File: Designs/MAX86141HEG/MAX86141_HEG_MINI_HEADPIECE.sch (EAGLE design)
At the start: 6 parts

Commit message: updates/another fix for boot routine
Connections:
- net GPIO1: now also JP4.6
- net GPIO2: now also JP4.5
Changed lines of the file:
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@@
 <setting verticaltext="up"/>
 </settings>
-<grid distance="10" unitdist="mil" unit="mil" style="lines" multiple="1" display="no" altdistance="0.01" altunitdist="inch" altunit="inch"/>
+<grid distance="0.01" unitdist="inch" unit="inch" style="lines" multiple="1" display="no" altdistance="0.01" altunitdist="inch" altunit="inch"/>
 <layers>
 <layer number="1" name="Top" color="4" fill="1" visible="no" active="no"/>
@@
 <label x="-25.146" y="91.948" size="1.778" layer="95"/>
 </segment>
+<segment>
+<pinref part="JP4" gate="A" pin="6"/>
+<wire x1="-86.614" y1="93.472" x2="-86.36" y2="93.472" width="0.1524" layer="91"/>
+<wire x1="-86.36" y1="93.472" x2="-86.36" y2="86.36" width="0.1524" layer="91"/>
+<label x="-87.63" y="86.106" size="1.778" layer="95" rot="R270"/>
+</segment>
 </net>
 <net name="GPIO2" class="0">
@@
 <label x="-25.146" y="89.662" size="1.778" layer="95"/>
 </segment>
+<segment>
+<pinref part="JP4" gate="A" pin="5"/>
+<wire x1="-89.154" y1="93.472" x2="-88.9" y2="93.472" width="0.1524" layer="91"/>
+<wire x1="-88.9" y1="93.472" x2="-88.9" y2="86.36" width="0.1524" layer="91"/>
+<label x="-90.17" y="85.852" size="1.778" layer="95" rot="R270"/>
+</segment>
 </net>

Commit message: quality improvements to design (hopefully)
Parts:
- added R1, R2: (no value), adafruit:R-US_0204/5
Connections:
- new net VLED1: JP4.16, R2.2
- new net VLED2: JP4.15, R1.2
- net LED1: now also R2.1; no longer JP4.16
- net LED2: now also R1.1; no longer JP4.15
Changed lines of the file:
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@@
 <?xml version="1.0" encoding="utf-8"?>
 <!DOCTYPE eagle SYSTEM "eagle.dtd">
-<eagle version="9.5.1">
+<eagle version="9.6.2">
 <drawing>
 <settings>
@@
 <part name="JP1" library="pinhead" library_urn="urn:adsk.eagle:library:325" deviceset="PINHD-1X16" device="" package3d_urn="urn:adsk.eagle:package:22432/2"/>
 <part name="JP4" library="pinhead" library_urn="urn:adsk.eagle:library:325" deviceset="PINHD-1X20" device="" package3d_urn="urn:adsk.eagle:package:22441/2"/>
+<part name="R1" library="adafruit" library_urn="urn:adsk.eagle:library:420" deviceset="R-US_" device="0204/5" package3d_urn="urn:adsk.eagle:package:6240595/1"/>
+<part name="R2" library="adafruit" library_urn="urn:adsk.eagle:library:420" deviceset="R-US_" device="0204/5" package3d_urn="urn:adsk.eagle:package:6240595/1"/>
 </parts>
 <sheets>
@@
 <attribute name="VALUE" x="-45.974" y="89.662" size="1.778" layer="96" rot="R90"/>
 </instance>
+<instance part="R1" gate="G$1" x="-63.754" y="81.28" smashed="yes" rot="R90">
+<attribute name="NAME" x="-65.2526" y="77.47" size="1.778" layer="95" rot="R90"/>
+<attribute name="VALUE" x="-60.452" y="77.47" size="1.778" layer="96" rot="R90"/>
+</instance>
+<instance part="R2" gate="G$1" x="-61.214" y="81.28" smashed="yes" rot="R90">
+<attribute name="NAME" x="-62.7126" y="77.47" size="1.778" layer="95" rot="R90"/>
+<attribute name="VALUE" x="-57.912" y="77.47" size="1.778" layer="96" rot="R90"/>
+</instance>
 </instances>
 <busses>
@@
 <pinref part="JP4" gate="A" pin="14"/>
 <wire x1="-66.294" y1="93.472" x2="-66.294" y2="87.122" width="0.1524" layer="91"/>
-<wire x1="-66.294" y1="87.122" x2="-66.04" y2="87.122" width="0.1524" layer="91"/>
 <label x="-65.278" y="75.946" size="1.778" layer="95" rot="R90"/>
 </segment>
@@
 </segment>
 <segment>
-<pinref part="JP4" gate="A" pin="15"/>
-<wire x1="-63.754" y1="93.472" x2="-63.754" y2="87.376" width="0.1524" layer="91"/>
-<wire x1="-63.754" y1="87.376" x2="-64.008" y2="87.376" width="0.1524" layer="91"/>
-<label x="-62.738" y="78.74" size="1.778" layer="95" rot="R90"/>
+<pinref part="R1" gate="G$1" pin="1"/>
+<wire x1="-63.754" y1="76.2" x2="-63.754" y2="74.93" width="0.1524" layer="91"/>
+<label x="-62.992" y="70.104" size="1.778" layer="95" rot="R90"/>
 </segment>
 </net>
@@
 </segment>
 <segment>
+<pinref part="R2" gate="G$1" pin="1"/>
+<wire x1="-61.214" y1="76.2" x2="-61.214" y2="75.184" width="0.1524" layer="91"/>
+<label x="-60.452" y="74.93" size="1.778" layer="95"/>
+</segment>
+</net>
+<net name="VLED1" class="0">
+<segment>
 <pinref part="JP4" gate="A" pin="16"/>
-<wire x1="-61.214" y1="93.472" x2="-61.214" y2="87.122" width="0.1524" layer="91"/>
-<label x="-60.198" y="78.74" size="1.778" layer="95" rot="R90"/>
-</segment>
-</net>
+<wire x1="-61.214" y1="93.472" x2="-61.214" y2="86.36" width="0.1524" layer="91"/>
+<label x="-60.452" y="98.044" size="1.778" layer="95" rot="R90"/>
+<pinref part="R2" gate="G$1" pin="2"/>
+</segment>
+</net>
+<net name="VLED2" class="0">
+<segment>
+<pinref part="JP4" gate="A" pin="15"/>
+<wire x1="-63.754" y1="93.472" x2="-63.754" y2="86.36" width="0.1524" layer="91"/>
+<label x="-63.246" y="97.79" size="1.778" layer="95" rot="R90"/>
+<pinref part="R1" gate="G$1" pin="2"/>
+</segment>
+</net>

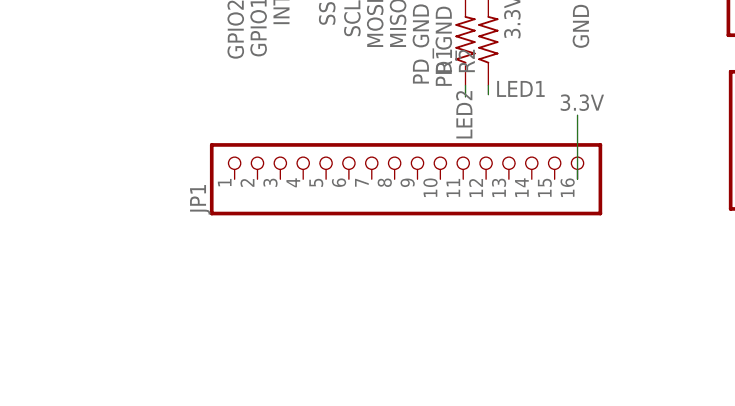
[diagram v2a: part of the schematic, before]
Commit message: headpiece update with switches
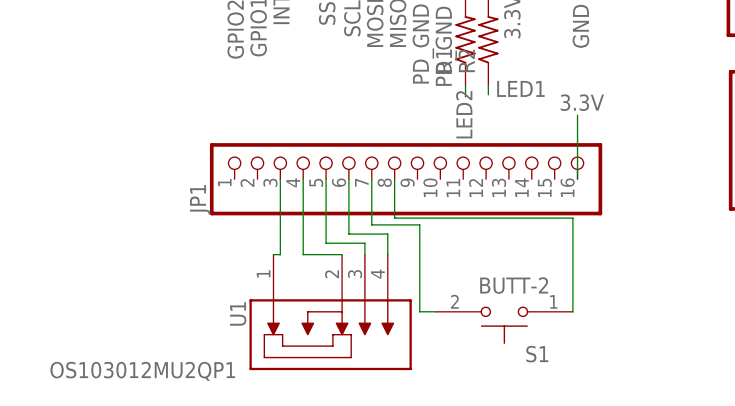
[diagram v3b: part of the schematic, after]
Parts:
- added S1: BUTT-2, BUTT-2:BUTT-2
- added U1: OS103012MU2QP1, OS103012MU2QP1:OS103012MU2QP1
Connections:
- new net N$1: JP1.3, U1.1
- new net N$2: JP1.4, U1.2
- new net N$3: JP1.5, U1.3
- new net N$4: JP1.6, U1.4
- new net N$5: JP1.7, S1.2
- new net N$6: JP1.8, S1.1
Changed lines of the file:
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@@
 <layer number="59" name="tCarbon" color="7" fill="1" visible="no" active="no"/>
 <layer number="60" name="bCarbon" color="7" fill="1" visible="no" active="no"/>
+<layer number="61" name="stand" color="7" fill="1" visible="no" active="no"/>
 <layer number="88" name="SimResults" color="9" fill="1" visible="yes" active="yes"/>
 <layer number="89" name="SimProbes" color="9" fill="1" visible="yes" active="yes"/>
@@
 <layer number="112" name="tSilk" color="7" fill="1" visible="no" active="yes"/>
 <layer number="113" name="ReferenceLS" color="7" fill="1" visible="no" active="no"/>
+<layer number="114" name="tValuesAlt" color="7" fill="1" visible="yes" active="yes"/>
+<layer number="115" name="ReferenceISLANDS" color="7" fill="1" visible="no" active="no"/>
 <layer number="116" name="Patch_BOT" color="9" fill="4" visible="no" active="yes"/>
+<layer number="117" name="BACKMAAT1" color="7" fill="1" visible="yes" active="yes"/>
 <layer number="118" name="Rect_Pads" color="7" fill="1" visible="no" active="no"/>
+<layer number="119" name="KAP_TEKEN" color="7" fill="1" visible="yes" active="yes"/>
+<layer number="120" name="KAP_MAAT1" color="7" fill="1" visible="yes" active="yes"/>
 <layer number="121" name="_tsilk" color="7" fill="1" visible="no" active="yes"/>
 <layer number="122" name="_bsilk" color="7" fill="1" visible="no" active="yes"/>
@@
 <layer number="128" name="_bValues" color="7" fill="1" visible="no" active="yes"/>
 <layer number="129" name="Mask" color="7" fill="1" visible="yes" active="yes"/>
+<layer number="130" name="bLogo" color="7" fill="1" visible="yes" active="yes"/>
 <layer number="131" name="tAdjust" color="7" fill="1" visible="no" active="yes"/>
 <layer number="132" name="bAdjust" color="7" fill="1" visible="no" active="yes"/>
+<layer number="133" name="bottom_silk" color="7" fill="1" visible="yes" active="yes"/>
+<layer number="134" name="silk_top" color="7" fill="1" visible="no" active="no"/>
+<layer number="135" name="silk_bottom" color="7" fill="1" visible="no" active="no"/>
+<layer number="136" name="silktop" color="7" fill="1" visible="yes" active="yes"/>
+<layer number="137" name="silkbottom" color="7" fill="1" visible="yes" active="yes"/>
 <layer number="144" name="Drill_legend" color="7" fill="1" visible="no" active="yes"/>
+<layer number="145" name="DrillLegend_01-16" color="7" fill="1" visible="yes" active="yes"/>
+<layer number="146" name="DrillLegend_01-20" color="7" fill="1" visible="yes" active="yes"/>
 <layer number="150" name="Notes" color="7" fill="1" visible="no" active="yes"/>
 <layer number="151" name="HeatSink" color="7" fill="1" visible="no" active="yes"/>
@@
 <layer number="154" name="FabDoc2" color="2" fill="1" visible="no" active="no"/>
 <layer number="155" name="FabDoc3" color="7" fill="15" visible="no" active="no"/>
+<layer number="166" name="AntennaArea" color="7" fill="1" visible="yes" active="yes"/>
+<layer number="168" name="4mmHeightArea" color="7" fill="1" visible="yes" active="yes"/>
 <layer number="199" name="Contour" color="7" fill="1" visible="no" active="yes"/>
 <layer number="200" name="200bmp" color="1" fill="10" visible="no" active="yes"/>
@@
 <part name="R1" library="adafruit" library_urn="urn:adsk.eagle:library:420" deviceset="R-US_" device="0204/5" package3d_urn="urn:adsk.eagle:package:6240595/1"/>
 <part name="R2" library="adafruit" library_urn="urn:adsk.eagle:library:420" deviceset="R-US_" device="0204/5" package3d_urn="urn:adsk.eagle:package:6240595/1"/>
+<part name="U1" library="OS103012MU2QP1" deviceset="OS103012MU2QP1" device=""/>
+<part name="S1" library="BUTT-2" deviceset="BUTT-2" device=""/>
 </parts>
 <sheets>
@@
 <attribute name="VALUE" x="-57.912" y="77.47" size="1.778" layer="96" rot="R90"/>
 </instance>
+<instance part="U1" gate="G$1" x="-80.01" y="49.784" smashed="yes" rot="MR270">
+<attribute name="NAME" x="-88.138" y="52.324" size="1.778" layer="95" rot="MR270"/>
+<attribute name="VALUE" x="-89.154" y="43.688" size="1.778" layer="96" rot="MR0"/>
+</instance>
+<instance part="S1" gate="G$1" x="-59.436" y="51.054" smashed="yes" rot="R180">
+<attribute name="NAME" x="-54.356" y="47.244" size="1.778" layer="95" rot="R180"/>
+<attribute name="VALUE" x="-54.356" y="54.864" size="1.778" layer="96" rot="R180"/>
+</instance>
 </instances>
 <busses>
@@
 </segment>
 </net>
+<net name="N$1" class="0">
+<segment>
+<pinref part="JP1" gate="A" pin="3"/>
+<pinref part="U1" gate="G$1" pin="1"/>
+<wire x1="-84.328" y1="65.786" x2="-84.328" y2="57.404" width="0.1524" layer="91"/>
+<wire x1="-84.328" y1="57.404" x2="-85.09" y2="57.404" width="0.1524" layer="91"/>
+</segment>
+</net>
+<net name="N$2" class="0">
+<segment>
+<pinref part="JP1" gate="A" pin="4"/>
+<pinref part="U1" gate="G$1" pin="2"/>
+<wire x1="-81.788" y1="65.786" x2="-81.788" y2="57.404" width="0.1524" layer="91"/>
+<wire x1="-81.788" y1="57.404" x2="-77.47" y2="57.404" width="0.1524" layer="91"/>
+</segment>
+</net>
+<net name="N$3" class="0">
+<segment>
+<pinref part="JP1" gate="A" pin="5"/>
+<wire x1="-79.248" y1="65.786" x2="-79.248" y2="58.674" width="0.1524" layer="91"/>
+<wire x1="-79.248" y1="58.674" x2="-74.93" y2="58.674" width="0.1524" layer="91"/>
+<pinref part="U1" gate="G$1" pin="3"/>
+<wire x1="-74.93" y1="58.674" x2="-74.93" y2="57.404" width="0.1524" layer="91"/>
+</segment>
+</net>
+<net name="N$4" class="0">
+<segment>
+<pinref part="JP1" gate="A" pin="6"/>
+<wire x1="-76.708" y1="65.786" x2="-76.708" y2="59.69" width="0.1524" layer="91"/>
+<pinref part="U1" gate="G$1" pin="4"/>
+<wire x1="-76.708" y1="59.69" x2="-72.39" y2="59.69" width="0.1524" layer="91"/>
+<wire x1="-72.39" y1="59.69" x2="-72.39" y2="57.404" width="0.1524" layer="91"/>
+</segment>
+</net>
+<net name="N$5" class="0">
+<segment>
+<pinref part="JP1" gate="A" pin="7"/>
+<wire x1="-74.168" y1="65.786" x2="-74.168" y2="60.706" width="0.1524" layer="91"/>
+<wire x1="-74.168" y1="60.706" x2="-68.834" y2="60.706" width="0.1524" layer="91"/>
+<wire x1="-68.834" y1="60.706" x2="-68.834" y2="51.054" width="0.1524" layer="91"/>
+<pinref part="S1" gate="G$1" pin="2"/>
+<wire x1="-68.834" y1="51.054" x2="-67.056" y2="51.054" width="0.1524" layer="91"/>
+</segment>
+</net>
+<net name="N$6" class="0">
+<segment>
+<pinref part="JP1" gate="A" pin="8"/>
+<wire x1="-71.628" y1="65.786" x2="-71.628" y2="61.468" width="0.1524" layer="91"/>
+<pinref part="S1" gate="G$1" pin="1"/>
+<wire x1="-71.628" y1="61.468" x2="-51.816" y2="61.468" width="0.1524" layer="91"/>
+<wire x1="-51.816" y1="61.468" x2="-51.816" y2="51.054" width="0.1524" layer="91"/>
+</segment>
+</net>

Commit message: fix
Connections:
- removed net N$6: JP1.8, S1.1
- net 3.3V: now also S1.1
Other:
- moved on the sheet: S1
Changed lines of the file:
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@@
 <attribute name="VALUE" x="-89.154" y="43.688" size="1.778" layer="96" rot="MR0"/>
 </instance>
-<instance part="S1" gate="G$1" x="-59.436" y="51.054" smashed="yes" rot="R180">
-<attribute name="NAME" x="-54.356" y="47.244" size="1.778" layer="95" rot="R180"/>
-<attribute name="VALUE" x="-54.356" y="54.864" size="1.778" layer="96" rot="R180"/>
+<instance part="S1" gate="G$1" x="-58.928" y="51.054" smashed="yes" rot="R180">
+<attribute name="NAME" x="-53.848" y="47.244" size="1.778" layer="95" rot="R180"/>
+<attribute name="VALUE" x="-53.848" y="54.864" size="1.778" layer="96" rot="R180"/>
 </instance>
 </instances>
@@
 <wire x1="-51.308" y1="65.786" x2="-51.308" y2="72.898" width="0.1524" layer="91"/>
 <label x="-53.34" y="73.406" size="1.778" layer="95"/>
+<pinref part="S1" gate="G$1" pin="1"/>
+<wire x1="-51.308" y1="65.786" x2="-51.308" y2="51.054" width="0.1524" layer="91"/>
+<junction x="-51.308" y="65.786"/>
 </segment>
 <segment>
@@
 <wire x1="-68.834" y1="60.706" x2="-68.834" y2="51.054" width="0.1524" layer="91"/>
 <pinref part="S1" gate="G$1" pin="2"/>
-<wire x1="-68.834" y1="51.054" x2="-67.056" y2="51.054" width="0.1524" layer="91"/>
-</segment>
-</net>
-<net name="N$6" class="0">
-<segment>
-<pinref part="JP1" gate="A" pin="8"/>
-<wire x1="-71.628" y1="65.786" x2="-71.628" y2="61.468" width="0.1524" layer="91"/>
-<pinref part="S1" gate="G$1" pin="1"/>
-<wire x1="-71.628" y1="61.468" x2="-51.816" y2="61.468" width="0.1524" layer="91"/>
-<wire x1="-51.816" y1="61.468" x2="-51.816" y2="51.054" width="0.1524" layer="91"/>
-</segment>
-</net>
+<wire x1="-68.834" y1="51.054" x2="-66.548" y2="51.054" width="0.1524" layer="91"/>
+</segment>
+</net>

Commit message: pushed firmware updates
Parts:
- removed U1: OS103012MU2QP1, OS103012MU2QP1:OS103012MU2QP1
- added S2: OS103011MS8QP1, OS103011MS8QP1:OS103011MS8QP1
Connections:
- removed net N$1: JP1.3, U1.1
- removed net N$2: JP1.4, U1.2
- removed net N$3: JP1.5, U1.3
- removed net N$4: JP1.6, U1.4
- new net 12: JP1.4, S2.C
- new net 13: JP1.3, S2.1
- new net 14: JP1.5, S2.2
- new net 27: JP1.6, S2.3
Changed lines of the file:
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@@
 <part name="R1" library="adafruit" library_urn="urn:adsk.eagle:library:420" deviceset="R-US_" device="0204/5" package3d_urn="urn:adsk.eagle:package:6240595/1"/>
 <part name="R2" library="adafruit" library_urn="urn:adsk.eagle:library:420" deviceset="R-US_" device="0204/5" package3d_urn="urn:adsk.eagle:package:6240595/1"/>
-<part name="U1" library="OS103012MU2QP1" deviceset="OS103012MU2QP1" device=""/>
 <part name="S1" library="BUTT-2" deviceset="BUTT-2" device=""/>
+<part name="S2" library="OS103011MS8QP1" deviceset="OS103011MS8QP1" device=""/>
 </parts>
 <sheets>
@@
 <attribute name="VALUE" x="-57.912" y="77.47" size="1.778" layer="96" rot="R90"/>
 </instance>
-<instance part="U1" gate="G$1" x="-80.01" y="49.784" smashed="yes" rot="MR270">
-<attribute name="NAME" x="-88.138" y="52.324" size="1.778" layer="95" rot="MR270"/>
-<attribute name="VALUE" x="-89.154" y="43.688" size="1.778" layer="96" rot="MR0"/>
-</instance>
 <instance part="S1" gate="G$1" x="-58.928" y="51.054" smashed="yes" rot="R180">
 <attribute name="NAME" x="-53.848" y="47.244" size="1.778" layer="95" rot="R180"/>
 <attribute name="VALUE" x="-53.848" y="54.864" size="1.778" layer="96" rot="R180"/>
+</instance>
+<instance part="S2" gate="G$1" x="-83.058" y="49.022" smashed="yes">
+<attribute name="NAME" x="-83.058" y="54.102" size="1.27" layer="95" ratio="12"/>
+<attribute name="VALUE" x="-83.058" y="43.942" size="1.27" layer="96" ratio="12"/>
 </instance>
 </instances>
@@
 </segment>
 </net>
-<net name="N$1" class="0">
+<net name="13" class="0">
 <segment>
 <pinref part="JP1" gate="A" pin="3"/>
-<pinref part="U1" gate="G$1" pin="1"/>
 <wire x1="-84.328" y1="65.786" x2="-84.328" y2="57.404" width="0.1524" layer="91"/>
-<wire x1="-84.328" y1="57.404" x2="-85.09" y2="57.404" width="0.1524" layer="91"/>
-</segment>
-</net>
-<net name="N$2" class="0">
-<segment>
-<pinref part="JP1" gate="A" pin="4"/>
-<pinref part="U1" gate="G$1" pin="2"/>
-<wire x1="-81.788" y1="65.786" x2="-81.788" y2="57.404" width="0.1524" layer="91"/>
-<wire x1="-81.788" y1="57.404" x2="-77.47" y2="57.404" width="0.1524" layer="91"/>
-</segment>
-</net>
-<net name="N$3" class="0">
-<segment>
-<pinref part="JP1" gate="A" pin="5"/>
-<wire x1="-79.248" y1="65.786" x2="-79.248" y2="58.674" width="0.1524" layer="91"/>
-<wire x1="-79.248" y1="58.674" x2="-74.93" y2="58.674" width="0.1524" layer="91"/>
-<pinref part="U1" gate="G$1" pin="3"/>
-<wire x1="-74.93" y1="58.674" x2="-74.93" y2="57.404" width="0.1524" layer="91"/>
-</segment>
-</net>
-<net name="N$4" class="0">
-<segment>
-<pinref part="JP1" gate="A" pin="6"/>
-<wire x1="-76.708" y1="65.786" x2="-76.708" y2="59.69" width="0.1524" layer="91"/>
-<pinref part="U1" gate="G$1" pin="4"/>
-<wire x1="-76.708" y1="59.69" x2="-72.39" y2="59.69" width="0.1524" layer="91"/>
-<wire x1="-72.39" y1="59.69" x2="-72.39" y2="57.404" width="0.1524" layer="91"/>
+<label x="-88.138" y="57.404" size="1.778" layer="95"/>
+</segment>
+<segment>
+<pinref part="S2" gate="G$1" pin="1"/>
+<wire x1="-72.898" y1="46.482" x2="-71.882" y2="46.482" width="0.1524" layer="91"/>
+<label x="-71.628" y="45.72" size="1.778" layer="95"/>
 </segment>
 </net>
@@
 </segment>
 </net>
+<net name="27" class="0">
+<segment>
+<pinref part="S2" gate="G$1" pin="3"/>
+<wire x1="-72.898" y1="51.562" x2="-71.882" y2="51.562" width="0.1524" layer="91"/>
+<label x="-71.628" y="51.054" size="1.778" layer="95"/>
+</segment>
+<segment>
+<pinref part="JP1" gate="A" pin="6"/>
+<wire x1="-76.708" y1="65.786" x2="-76.708" y2="59.69" width="0.1524" layer="91"/>
+<wire x1="-76.708" y1="59.69" x2="-72.39" y2="59.69" width="0.1524" layer="91"/>
+<wire x1="-72.39" y1="59.69" x2="-72.39" y2="56.388" width="0.1524" layer="91"/>
+<label x="-72.898" y="54.864" size="1.778" layer="95"/>
+</segment>
+</net>
+<net name="14" class="0">
+<segment>
+<pinref part="S2" gate="G$1" pin="2"/>
+<wire x1="-72.898" y1="49.022" x2="-71.882" y2="49.022" width="0.1524" layer="91"/>
+<label x="-71.882" y="48.514" size="1.778" layer="95"/>
+</segment>
+<segment>
+<pinref part="JP1" gate="A" pin="5"/>
+<wire x1="-79.248" y1="65.786" x2="-79.248" y2="58.674" width="0.1524" layer="91"/>
+<wire x1="-79.248" y1="58.674" x2="-74.93" y2="58.674" width="0.1524" layer="91"/>
+<wire x1="-74.93" y1="58.674" x2="-74.93" y2="56.388" width="0.1524" layer="91"/>
+<label x="-76.454" y="55.88" size="1.778" layer="95"/>
+</segment>
+</net>
+<net name="12" class="0">
+<segment>
+<pinref part="S2" gate="G$1" pin="C"/>
+<wire x1="-85.598" y1="49.022" x2="-87.376" y2="49.022" width="0.1524" layer="91"/>
+<label x="-90.932" y="49.022" size="1.778" layer="95"/>
+</segment>
+<segment>
+<pinref part="JP1" gate="A" pin="4"/>
+<wire x1="-81.788" y1="65.786" x2="-81.788" y2="57.404" width="0.1524" layer="91"/>
+<label x="-83.058" y="56.896" size="1.778" layer="95"/>
+</segment>
+</net>
